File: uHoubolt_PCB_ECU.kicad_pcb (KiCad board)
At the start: 4 copper layers, 60 x 60 mm, 201 parts, among them J1 Power In, J10 OUT 1, J11 PYRO 1, J12 Pressure 1, J13 Pressure 1, J14 Pressure 1, J15 Pressure 1, J16 TEMP 1, J17 TEMP 1, J18 Servo 1, J19 Servo 1, J2 Debug, J20 OUT 1, J21 PYRO 1, J22 PYRO 1, J3 CAN1, J4 CAN2, J5 CAN1, J6 CAN2, J7 Pressure 1, J8 TEMP 1, J9 Servo 1, Q1 SISA88DN or similar, Q2 SISA88DN or similar, U1 SiC431C, U10 INA180B1, U11 TPS1HC100, U12 INA180B1, U13 INA180B1, U14 INA180B1, U15 INA180B1, U16 INA180B1, U17 INA180B1, U18 TPS1HC100, U19 TPS1HC100, U2 TS30041-M050QFNR, U3 MCP1700-3302E, U4 MCP2562FDT-H_SN, U5 MCP2562FDT, U6 STM32G491MET6-LQFP80, U7 ICM-20602, U8 W25Q256JV, U9 INA180B1, X1 TXC-7C

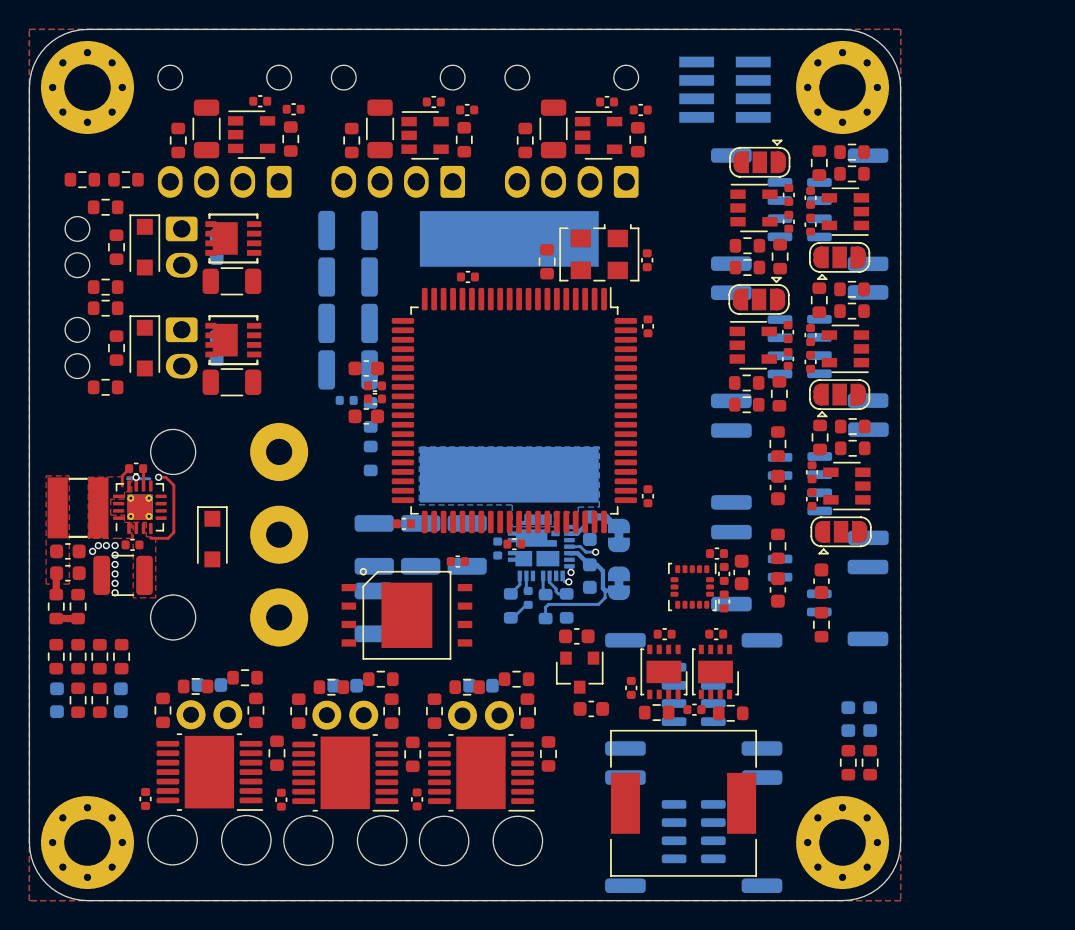
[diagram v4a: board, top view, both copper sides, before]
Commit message: changed form factor to better fit into uHb engine section
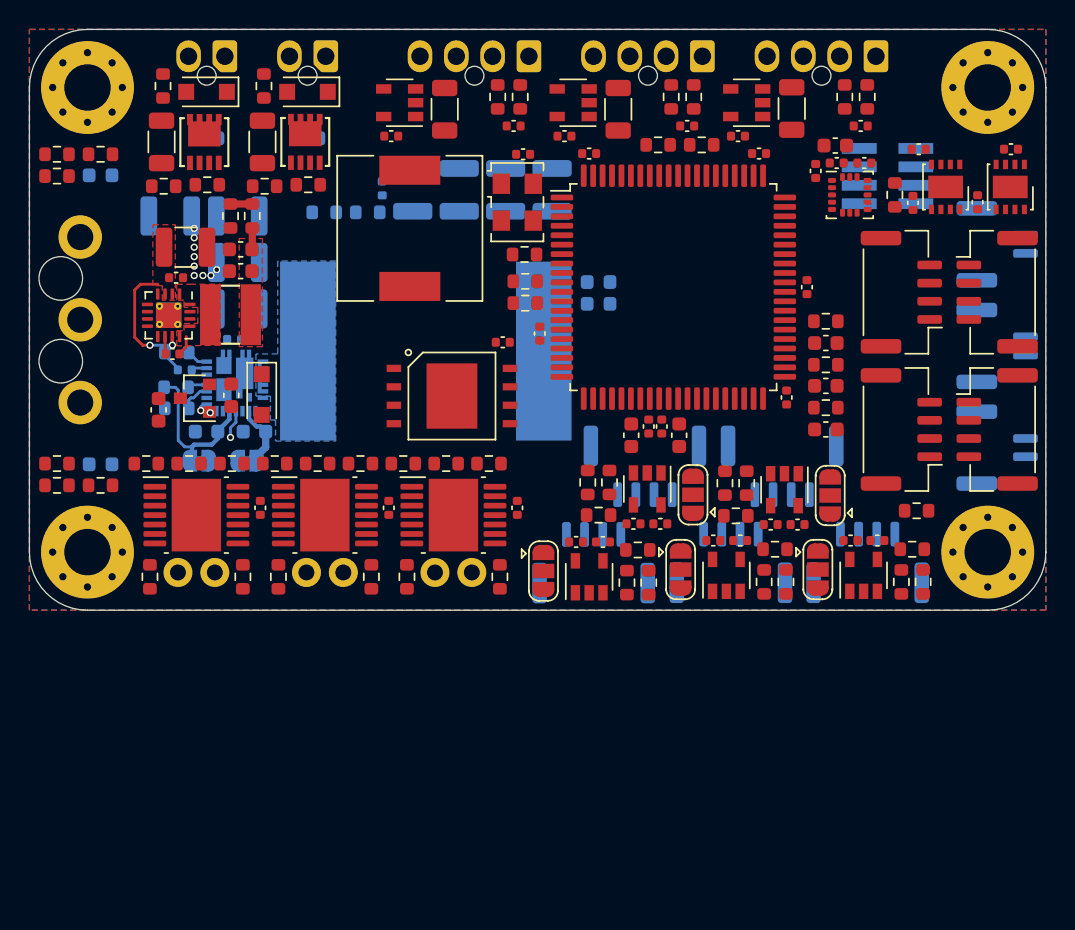
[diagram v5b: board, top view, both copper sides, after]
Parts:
- J1: footprint TXV_LIB:Molex_MegaFit_1x03 -> TXV_LIB:Molex_MegaFit_1x03_Vertical
- J10, J20: footprint TXV_LIB:Molex_Nano-Fit_105313-xx02_1x02_P2.50mm_Horizontal -> TXV_LIB:Molex_Nano-Fit_105309-xx02_1x02_P2.50mm_Vertical
- J11, J21, J22: footprint TXV_LIB:Molex_SL_1x2 -> TXV_LIB:Molex_SL_1x2_Vertical
- J18, J19, J9: footprint TXV_LIB:Molex_Nano-Fit_105313-xx04_1x04_P2.50mm_Horizontal -> TXV_LIB:Molex_Nano-Fit_105309-xx04_1x04_P2.50mm_Vertical
- J3, J4, J5, J6: moved to F.Cu
- moved R27 46.0 mm to (176.2, 84.7), turned to 90 degrees
- moved LS1 43.9 mm to (146.2, 93.7), turned to 0 degrees
- moved R13 42.7 mm to (166.3, 88.0), turned to 0 degrees
- moved J9 42.0 mm to (178.3, 81.8)
- moved R26 40.3 mm to (172.5, 85.5), turned to 270 degrees
- moved C21 40.0 mm to (185.3, 91.9), turned to 90 degrees
- moved R20 39.9 mm to (154.2, 97.3), turned to 180 degrees
- moved R25 39.8 mm to (177.7, 84.7), turned to 90 degrees
- moved R19 39.6 mm to (154.2, 98.8), turned to 180 degrees
- moved R18 39.2 mm to (179.6, 91.4), turned to 270 degrees
- moved U4 39.1 mm to (187.6, 90.8)
- moved C26 39.1 mm to (187.6, 88.2)
- moved C43 39.1 mm to (177.2, 86.7)
- moved U5 38.6 mm to (183.1, 90.8)
- moved C22 38.6 mm to (180.8, 92.0)
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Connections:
- J11 pad 1: Net-(J11-Pad1) -> GND
- J11 pad 2: GND -> Net-(J11-Pad2)
- J21 pad 1: Net-(J21-Pad1) -> GND
- J21 pad 2: GND -> Net-(J21-Pad2)
- J22 pad 1: Net-(J22-Pad1) -> GND
- J22 pad 2: GND -> Net-(J22-Pad2)
- R34 pad 1: Net-(J11-Pad1) -> Net-(J11-Pad2)
- R36 pad 2: Net-(J11-Pad1) -> Net-(J11-Pad2)
- R63 pad 1: Net-(J21-Pad1) -> Net-(J21-Pad2)
- R65 pad 2: Net-(J21-Pad1) -> Net-(J21-Pad2)
- R68 pad 1: Net-(J22-Pad1) -> Net-(J22-Pad2)
- R70 pad 2: Net-(J22-Pad1) -> Net-(J22-Pad2)
- U11 pad 10: Net-(J11-Pad1) -> Net-(J11-Pad2)
- U11 pad 8: Net-(J11-Pad1) -> Net-(J11-Pad2)
- U11 pad 9: Net-(J11-Pad1) -> Net-(J11-Pad2)
- U18 pad 10: Net-(J21-Pad1) -> Net-(J21-Pad2)
- U18 pad 8: Net-(J21-Pad1) -> Net-(J21-Pad2)
- U18 pad 9: Net-(J21-Pad1) -> Net-(J21-Pad2)
- U19 pad 10: Net-(J22-Pad1) -> Net-(J22-Pad2)
- U19 pad 8: Net-(J22-Pad1) -> Net-(J22-Pad2)
- U19 pad 9: Net-(J22-Pad1) -> Net-(J22-Pad2)
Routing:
- net +12V: vias 2 -> 5
- net GND: vias 9 -> 6
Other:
- board size 60 x 60 mm -> 70 x 40 mm
- board text added: "7V4 SMPS"

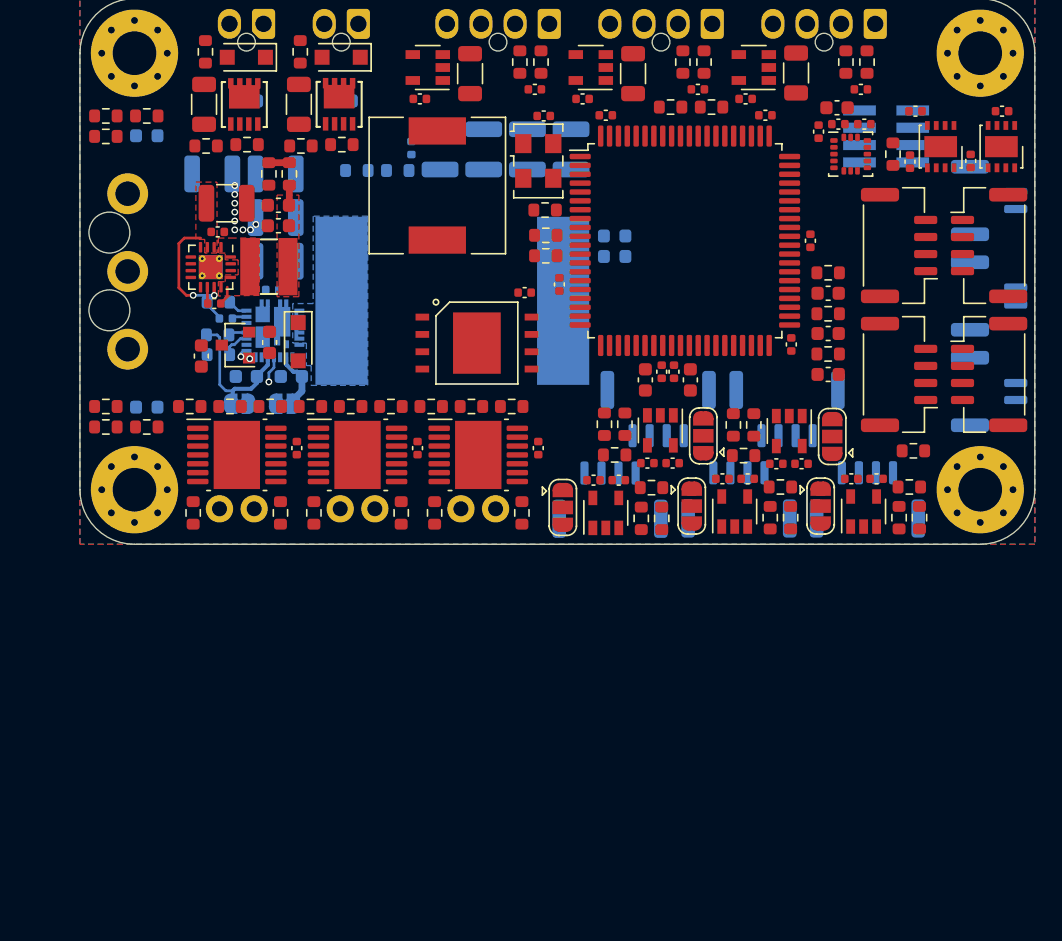
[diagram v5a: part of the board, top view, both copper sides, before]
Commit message: moved 7V4 buck to separate board
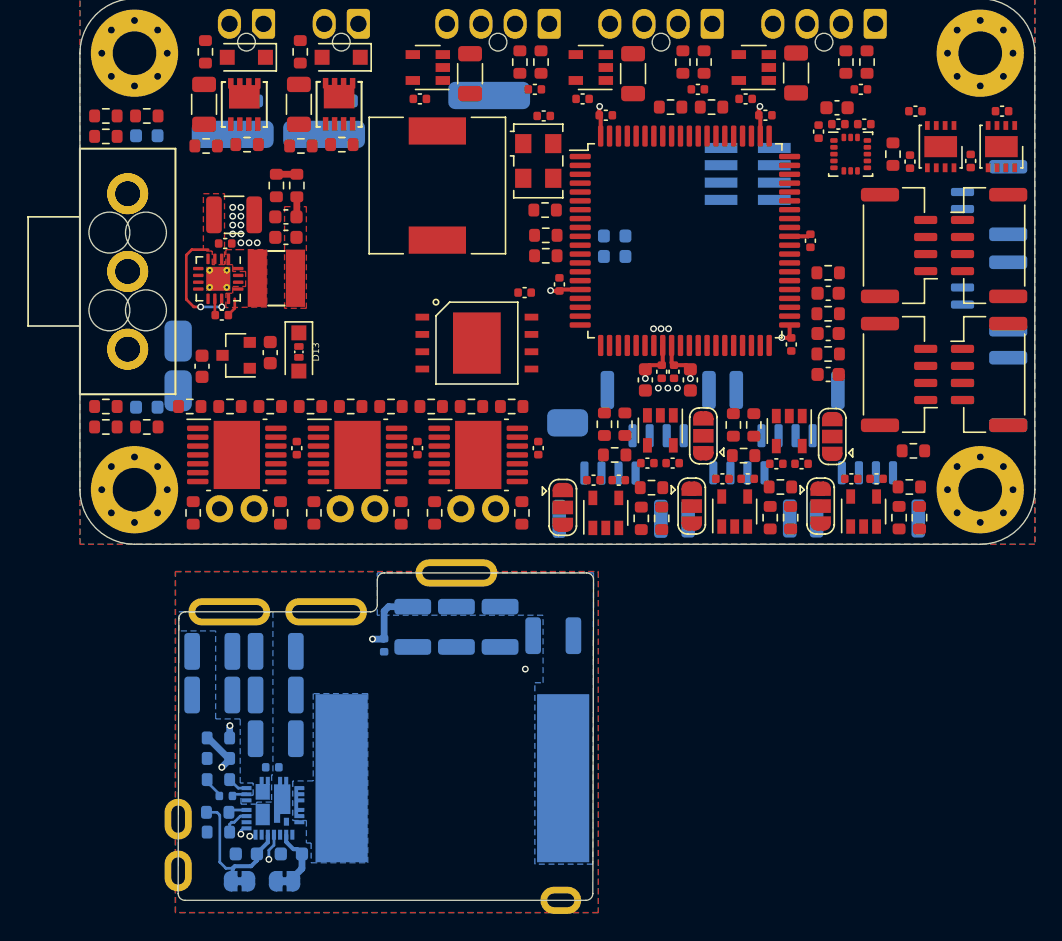
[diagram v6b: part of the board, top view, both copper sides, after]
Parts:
- added C62: 100µ, Capacitor_SMD:C_1210_3225Metric, B.Cu at (129.7, 131.1)
- added D13: TVS Uni, TXV_LIB:SOD882D, F.Cu at (136.1, 105.9)
- added J1: Power In, TXV_LIB:Molex_MegaFit_1x03_Vertical, F.Cu at (123.5, 100.0)
- added J23: 12V, TXV_LIB:PlatedEdgePad_6mm, B.Cu at (131.2, 90.0)
- added J24: 7V4_EN, TXV_LIB:PlatedEdgePad_3mm, B.Cu at (127.2, 105.1)
- added J25: GND, TXV_LIB:PlatedEdgePad_6mm, B.Cu at (137.9, 90.0)
- added J26: 7V4, TXV_LIB:PlatedEdgePad_6mm, B.Cu at (150.0, 87.1)
- added J27: 7V4_PGOOD, TXV_LIB:PlatedEdgePad_3mm, B.Cu at (155.8, 111.1)
- added J28: 12V, TXV_LIB:PlatedEdge_6mm, F.Cu at (130.9, 125.0)
- added J29: GND, TXV_LIB:PlatedEdge_6mm, F.Cu at (138.1, 125.0)
- added J30: 7V4_EN, TXV_LIB:PlatedEdge_3mm, F.Cu at (127.2, 140.2)
- added J31: 7V4_PGOOD, TXV_LIB:PlatedEdge_3mm, F.Cu at (155.2, 146.1)
- added J32: 7V4, TXV_LIB:PlatedEdge_6mm, F.Cu at (147.6, 122.1)
- added J33: 5V, TXV_LIB:PlatedEdgePad_3mm, B.Cu at (127.2, 108.8)
- added J34: 5V, TXV_LIB:PlatedEdge_3mm, F.Cu at (127.2, 143.9)
- R36, R65, R70: value 22k -> 100k
- moved R11 44.3 mm to (130.2, 135.7)
- moved R10 43.6 mm to (130.2, 134.2)
- moved C9 36.5 mm to (142.3, 127.4), turned to 270 degrees
- moved C15 35.7 mm to (154.7, 126.7), turned to 180 degrees
- moved C11 35.1 mm to (144.4, 126.0), turned to 270 degrees
- moved C13 35.1 mm to (147.6, 126.0), turned to 270 degrees
- moved C14 35.1 mm to (150.8, 126.0), turned to 270 degrees
- moved C5 35.0 mm to (134.3, 131.1)
- moved C1 35.0 mm to (129.7, 127.8)
- moved C2 35.0 mm to (134.3, 127.8)
- moved C6 35.0 mm to (134.3, 134.2)
- moved C7 35.0 mm to (134.1, 136.3)
- moved L1 35.0 mm to (147.3, 137.2)
- moved R1 35.0 mm to (130.1, 139.7)
- moved R2 35.0 mm to (130.2, 141.1)
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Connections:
- U1 pad 14: /7V4_PGOOD -> Net-(J31-Pad1)
- U1 pad 19: /7V4_EN -> Net-(J30-Pad1)
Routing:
- net +7.4V: track 0.73 -> 32.6 mm, vias 1 -> 3
- net +3V3: track 0.00 -> 17.0 mm, vias 0 -> 6
- net Net-(R10-Pad1): track 0.47 -> 9.55 mm, vias 1 -> 2
- net Net-(J31-Pad1): track 0.00 -> 1.97 mm, vias 0 -> 1
- net /7V4_PGOOD: track 1.97 -> 0.00 mm, vias 1 -> 0
- net +12V: vias 5 -> 2
- net GND: vias 6 -> 18
- added copper zone on B.Cu, net +12V
- added copper zone on In2.Cu, net +3V3
- added copper zone on B.Cu, net +7.4V
- added copper zone on In1.Cu, net GND
- added copper zone on In2.Cu, net GND
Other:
- board size 70 x 40 mm -> 70 x 66.1 mm
- board text added: "ToDo: Buck Board Outline & Pads anpassen"

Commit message: many small changes, before removing servo buck converter
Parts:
- added J35: CAN1, Connector_JST:JST_GH_BM04B-GHS-TBT_1x04-1MP_P1.25mm_Vertical, B.Cu at (186.7, 101.7)
- added J36: CAN2, Connector_JST:JST_GH_BM04B-GHS-TBT_1x04-1MP_P1.25mm_Vertical, B.Cu at (186.7, 92.2)
- added J37: CAN1, Connector_JST:JST_GH_BM04B-GHS-TBT_1x04-1MP_P1.25mm_Vertical, B.Cu at (180.1, 101.7)
- added J38: CAN2, Connector_JST:JST_GH_BM04B-GHS-TBT_1x04-1MP_P1.25mm_Vertical, B.Cu at (180.1, 92.2)
- added R71: 9k1, Resistor_SMD:R_0603_1608Metric, F.Cu at (198.8, 84.2)
- added R72: 9k1, Resistor_SMD:R_0603_1608Metric, F.Cu at (198.7, 90.6)
- added R73: 9k1, Resistor_SMD:R_0603_1608Metric, F.Cu at (199.3, 75.0)
- R33, R62, R67: value 22k -> 56k
- moved R19 46.3 mm to (190.6, 70.3)
- moved R20 46.3 mm to (190.6, 68.8)
- moved D4 39.2 mm to (185.9, 70.2)
- moved D5 39.2 mm to (185.9, 68.7)
- moved J16 38.8 mm to (222.3, 93.6), turned to 180 degrees
- moved C55 34.0 mm to (199.3, 78.0)
- moved R50 34.0 mm to (199.3, 76.5)
- moved R16 31.3 mm to (171.1, 69.2)
- moved J8 29.8 mm to (215.3, 93.6), turned to 180 degrees
- moved C42 29.6 mm to (198.8, 87.1)
- moved R24 29.6 mm to (198.8, 85.7)
- moved C54 27.7 mm to (198.7, 93.5)
- moved R49 27.7 mm to (198.7, 92.0)
- moved J2 24.8 mm to (177.2, 69.5)
- moved J17 21.7 mm to (208.3, 93.6), turned to 180 degrees
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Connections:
- net /TEMP_1 renamed Net-(C42-Pad2)
- net /TEMP_2 renamed Net-(C54-Pad2)
- net /TEMP_3 renamed Net-(C55-Pad2)

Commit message: placement almost done
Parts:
- removed C11, C13, C14, C15, C5, C6, C62: 100µ, Capacitor_SMD:C_1210_3225Metric
- removed C3: 22µ, Capacitor_SMD:C_0603_1608Metric
- removed C4: 2µ2, Capacitor_SMD:C_0603_1608Metric
- removed C7, C8, C9: 100n, Capacitor_SMD:C_0402_1005Metric
- removed J27: 7V4_PGOOD, TXV_LIB:PlatedEdgePad_3mm
- removed J28: 12V, TXV_LIB:PlatedEdge_6mm
- removed J29: GND, TXV_LIB:PlatedEdge_6mm
- removed J30: 7V4_EN, TXV_LIB:PlatedEdge_3mm
- removed J31: 7V4_PGOOD, TXV_LIB:PlatedEdge_3mm
- removed J32: 7V4, TXV_LIB:PlatedEdge_6mm
- removed J33: 5V, TXV_LIB:PlatedEdgePad_3mm
- removed J34: 5V, TXV_LIB:PlatedEdge_3mm
- removed JP2: VDD, Jumper:SolderJumper-2_P1.3mm_Bridged_RoundedPad1.0x1.5mm
- removed L1: 820nH, Inductor_SMD:L_Vishay_IHLP-6767
- added D14: OUT 1, LED_SMD:LED_0603_1608Metric, B.Cu at (174.6, 87.5)
- added D15: OUT 1, LED_SMD:LED_0603_1608Metric, B.Cu at (150.7, 87.5)
- added D16: OUT 1, LED_SMD:LED_0603_1608Metric, B.Cu at (162.6, 87.5)
- added D17: 3V3, LED_SMD:LED_0603_1608Metric, B.Cu at (129.2, 91.7)
- added F1: 350mA, Fuse:Fuse_1206_3216Metric, F.Cu at (133.8, 96.7)
- added F2: 350mA, Fuse:Fuse_1206_3216Metric, F.Cu at (130.8, 107.5)
- added G***: LOGO, TXV_LIB:ST_Logo_new, B.Cu at (166.5, 97.2)
- added R74: 120, Resistor_SMD:R_0603_1608Metric, F.Cu at (162.7, 85.7)
- added R75: 1k, Resistor_SMD:R_0603_1608Metric, F.Cu at (127.8, 96.5)
- added R76: 1k, Resistor_SMD:R_0603_1608Metric, F.Cu at (128.4, 93.5)
- added U20: D1213A-04V, Package_TO_SOT_SMD:SOT-563, F.Cu at (198.8, 119.2)
- C1, C2: value 100µ -> 100n; footprint Capacitor_SMD:C_1210_3225Metric -> Capacitor_SMD:C_0402_1005Metric; moved to F.Cu
- C10: value 100µ -> 10µ; footprint Capacitor_SMD:C_1210_3225Metric -> Capacitor_SMD:C_0805_2012Metric
- D13: value TVS Uni -> TVS 3V3
- D3: value TVS Uni -> 5V; footprint Diode_SMD:D_SOD-123F -> LED_SMD:LED_0603_1608Metric; moved to B.Cu
- J23: value 12V -> Pressure 1; footprint TXV_LIB:PlatedEdgePad_6mm -> Connector_JST:JST_GH_BM04B-GHS-TBT_1x04-1MP_P1.25mm_Vertical
- J24: value 7V4_EN -> 12V; footprint TXV_LIB:PlatedEdgePad_3mm -> TXV_LIB:PlatedEdgePad_6mm
- J26: value 7V4 -> Servo
- JP3: value VDRV -> V_SEL; footprint Jumper:SolderJumper-2_P1.3mm_Bridged_RoundedPad1.0x1.5mm -> Jumper:SolderJumper-3_P1.3mm_Open_RoundedPad1.0x1.5mm; moved to F.Cu
- R1: value 100k -> 4k7/0; moved to F.Cu
- R10: value 100k -> 120; moved to F.Cu
- R11: value 9k1 -> 120; moved to F.Cu
- R12: value 22k -> 9k1
- R13: value 9k1 -> 1k
- R2: value 200k -> 6k8/160; moved to F.Cu
- R7: value 3R3 -> 9k1; moved to F.Cu
- U1: value SiC431C -> INA180B1; footprint TXV_LIB:SiC431AEDT1GE3 -> Package_TO_SOT_SMD:SOT-23-5; moved to F.Cu
- moved R10 65.8 mm to (174.6, 85.7), turned to 90 degrees
- moved R11 54.1 mm to (150.7, 85.7), turned to 90 degrees
- moved J36 50.7 mm to (136.2, 96.7), turned to 180 degrees
- moved R13 46.3 mm to (134.6, 106.3), turned to 180 degrees
- moved R12 45.5 mm to (134.6, 107.8)
- moved J38 45.2 mm to (136.2, 103.3), turned to 0 degrees
- moved JP3 44.6 mm to (162.2, 112.2), turned to 90 degrees
- moved J35 41.3 mm to (145.7, 96.7), turned to 180 degrees
- moved R19 40.4 mm to (178.3, 108.8)
- moved R20 40.4 mm to (178.3, 107.3)
- moved R2 38.7 mm to (154.9, 111.3), turned to 90 degrees
- moved R1 38.7 mm to (156.4, 111.3), turned to 270 degrees
- moved J16 37.4 mm to (186.7, 105.0), turned to 90 degrees
- moved U1 37.1 mm to (159.0, 111.8)
- moved D4 35.8 mm to (178.1, 105.2), turned to 0 degrees
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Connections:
- net /7V4_SENSE renamed /12VA_SENSE
- net Net-(U2-Pad8) renamed /5V_PGOOD
- C1 pad 1: +12V -> +3V3
- C16 pad 2: +5V -> /5V_unfused
- C18 pad 1: +5V -> /5V_unfused
- C19 pad 1: +5V -> /5V_unfused
- C2 pad 1: +12V -> /PRESS_6
- C26 pad 1: +5V -> /5V_unfused
- C27 pad 1: +5V -> /5V_unfused
- D3 pad 1: +3V3 -> GND
- D3 pad 2: GND -> Net-(D3-Pad2)
- J23 pad 1: +12V -> Net-(J23-Pad1)
- J24 pad 1: /7V4_EN -> +12V
- J26 pad 1: +7.4V -> VS
- JP1 pad 3: +12V -> +12VA
- JP3 pad 2: Net-(C4-Pad1) -> Net-(J23-Pad1)
- JP4 pad 3: +12V -> +12VA
- JP5 pad 3: +12V -> +12VA
- JP6 pad 3: +12V -> +12VA
- JP7 pad 3: +12V -> +12VA
- L2 pad 2: +5V -> /5V_unfused
- R1 pad 1: Net-(R1-Pad1) -> Net-(J23-Pad2)
- R1 pad 2: Net-(C4-Pad1) -> Net-(R1-Pad2)
- R10 pad 1: Net-(R10-Pad1) -> /SERVO_1_LED
- R10 pad 2: +7.4V -> Net-(D14-Pad2)
- R11 pad 1: GND -> /SERVO_2_LED
- R11 pad 2: Net-(R10-Pad1) -> Net-(D15-Pad2)
- R12 pad 1: +7.4V -> +12VA
- R2 pad 1: GND -> Net-(R1-Pad2)
- R2 pad 2: Net-(R2-Pad2) -> GND
- R26 pad 2: +7.4V -> VS
- R52 pad 2: +7.4V -> VS
- R55 pad 2: +7.4V -> VS
- R7 pad 1: Net-(C8-Pad1) -> Net-(R1-Pad2)
- R7 pad 2: Net-(R7-Pad2) -> /PRESS_6
- U1 pad 1: +12V -> Net-(J23-Pad2)
- U1 pad 2: +12V -> GND
- U1 pad 3: GND -> Net-(J23-Pad3)
- U1 pad 4: GND -> Net-(R1-Pad2)
- U1 pad 5: Net-(L1-Pad1) -> +3V3
- U10 pad 1: +7.4V -> VS
- U16 pad 1: +7.4V -> VS
- U17 pad 1: +7.4V -> VS
- U2 pad 5: +5V -> /5V_unfused
- U3 pad 3: +5V -> /5V_unfused
- U4 pad 3: +5V -> /5V_unfused
- U5 pad 3: +5V -> /5V_unfused
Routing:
- net +7.4V: track 32.6 -> 0.00 mm, vias 3 -> 0
- net Net-(C4-Pad1): track 10.8 -> 0.00 mm
- net Net-(R10-Pad1): track 9.55 -> 0.00 mm, vias 2 -> 0
- net /5V_unfused: track 0.00 -> 8.17 mm, vias 0 -> 2
- net Net-(C3-Pad1): track 4.31 -> 0.00 mm
- net Net-(R2-Pad2): track 2.06 -> 0.00 mm
- net Net-(J31-Pad1): track 1.97 -> 0.00 mm, vias 1 -> 0
- net Net-(C8-Pad1): track 1.70 -> 0.00 mm
- net +5V: track 1.63 -> 0.00 mm
- net /5V_SENSE: track 1.50 -> 0.00 mm
- net Net-(R7-Pad2): track 1.50 -> 0.00 mm
- net Net-(R1-Pad1): track 1.31 -> 0.00 mm
- net Net-(C8-Pad2): track 1.08 -> 0.00 mm
- net GND: vias 18 -> 16
- added copper zone on F.Cu, net /5V_unfused
- removed copper zone on B.Cu, net +12V
- removed copper zone on F.Cu, net +5V
- removed copper zone on B.Cu, net +7.4V
- removed copper zone on In2.Cu, net GND
- removed copper zone on B.Cu, net Net-(L1-Pad1)
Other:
- board size 70 x 66.1 mm -> 70 x 40 mm
- board text added: "0"
- board text added: "1"
- board text added: "2"
- board text added: "3"
- board text added: "4"
- board text added: "5"
- board text added: "CAN1"
- board text added: "CAN2"
- board text added: "Debug"
- board text added: "ECU"
- board text added: "Pressure"
- board text added: "Pyro 0"
- board text added: "Pyro 1"
- board text added: "Pyro 2"
- board text added: "Servo 0"
- board text added: "Servo 1"
- board text added: "Servo 2"
- board text added: "Solenoid"
- board text added: "Status"
- board text added: "Temperature"
- board text added: "v1.0"
- board text removed: "7V4 SMPS"
- board text removed: "ToDo: Buck Board Outline & Pads anpassen"
